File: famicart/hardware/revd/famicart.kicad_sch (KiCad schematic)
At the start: 134 parts, among them J1 Famicom 60-pin edge, J2 RUN/GND, J3 USB-C PRG/mapper (U1) (HRO TY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, J4 USB-C CHR (U2) (HRO TYPE-C-31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, J5 SWD A (SWCLK GND SWDIO), J6 SWD B (SWCLK GND SWDIO), SW1 RESET, SW2 BOOTSEL A, SW3 BOOTSEL B, U1 RP2350B, U10 74LVC541 U10, U11 74LVC541 U11, U12 74LVC245 CPU data (console<->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, U13 74LVC1G11 AND3: CPU data enab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, U14 74LVC1G32 OR: CPU 245 /OE, U15 74LVC1G04 INV: R/W, U16 74LVC1G00 NAND: WRAM /WE, U17 74LVC541 U17, U18 74LVC541 U18, U19 74LVC245 PPU data (console<->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, U2 RP2350B, U20 74LVC00 PPU access / CIRAM gl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, U21 74LVC1G32 OR: PPU 245 /OE, U22 74LVC139 CHR ROM/RAM select, U24 74LVC245 CPU->PPU data bridge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, U26 74LVC1G07 OD: /IRQ A, U27 74LVC1G07 OD: /IRQ B, U28 AMS1117-3.3, U3 W25Q16JVSSIQ, U4 W25Q16JVSSIQ, U5 S29GL01GS 1Gbit NOR (x8 use), U6 S29GL01GS 1Gbit NOR (x8 use), U7 IS62WV5128 512Kx8 SRAM, U8 IS62WV5128 512Kx8 SRAM, U9 74LVC541 U9, Y1 12MHz ABM8-272-T3, Y2 12MHz ABM8-272-T3

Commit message: famicart rev D: boot-bank pull-ups, F-RAM save RAM, U1 GPIO remap for PIO-driven nDRIVE
Target is a cartridge that works in a real Famicom: PRG bank lines are pulled up so the
console boots from a fixed top bank (boot stub) before the MCUs are up; WRAM becomes a
128 KB FM28V100 F-RAM (non-volatile saves without a battery); nDRIVE moves into PIO0's
GPIO window so the data-drive path can assert it by side-set.

Co-Authored-By: Claude Fable 5.1 <noreply@anthropic.com>
Claude-Session: https://claude.ai/code/session_01RfF2rUHDV6Gz9CaznXPSPp
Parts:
- removed U7: IS62WV5128 512Kx8 SRAM, Package_SO:TSOP-I-32_11.8x8mm_P0.5mm, symbol famicart:IS62WV5128_sTSOP32
- added R26: 1k, Resistor_SMD:R_0603_1608Metric, symbol Device:R
- added RN7, RN8, RN9: 10k x4, Resistor_SMD:R_Array_Convex_4x0603, symbol Device:R_Pack04
- added U7: FM28V100 128Kx8 F-RAM (WRAM/save), Package_SO:TSOP-I-32_11.8x8mm_P0.5mm, symbol famicart:FM28V100_TSOP32
- R25: value 1k -> 10k
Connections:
- net +3V3: now also R25.2, RN7.5 (R4.2), RN7.6 (R3.2), RN7.7 (R2.2), RN7.8 (R1.2), RN8.5 (R4.2), RN8.6 (R3.2), RN8.7 (R2.2), RN8.8 (R1.2), RN9.5 (R4.2), RN9.6 (R3.2), RN9.7 (R2.2), RN9.8 (R1.2), U7.6 (CE2), U7.8 (VDD)
- net CA0: now also U7.20 (A0)
- net CA1: now also U7.19 (A1)
- net CA10: now also U7.31 (A10)
- net CA11: now also U7.1 (A11)
- net CA12: now also U7.12 (A12)
- net CA2: now also U7.18 (A2)
- net CA3: now also U7.17 (A3)
- net CA4: now also U7.16 (A4)
- net CA5: now also U7.15 (A5)
- net CA6: now also U7.14 (A6)
- net CA7: now also U7.13 (A7)
- net CA8: now also U7.3 (A8)
- net CA9: now also U7.2 (A9)
- net CD0: now also U7.21 (DQ0)
- net CD1: now also U7.22 (DQ1)
- net CD2: now also U7.23 (DQ2)
- net CD3: now also U7.25 (DQ3)
- net CD4: now also U7.26 (DQ4)
- net CD5: now also U7.27 (DQ5)
- net CD6: now also U7.28 (DQ6)
- net CD7: now also U7.29 (DQ7)
- net CRWn: now also U7.32 (OE#)
- net GND: now also U7.24 (VSS)
- net LED: now also R26.1; no longer R25.1
- net LED_A: now also R26.2; no longer R25.2
- net PRG_A13: now also U1.28 (GPIO27), RN7.1 (R1.1), U7.4 (A13); no longer U1.27 (GPIO26)
- net PRG_A14: now also U1.36 (GPIO28), RN7.2 (R2.1), U7.11 (A14); no longer U1.28 (GPIO27)
- net PRG_A15: now also U1.37 (GPIO29), RN7.3 (R3.1), U7.7 (A15); no longer U1.36 (GPIO28)
- net PRG_A16: now also U1.38 (GPIO30), RN7.4 (R4.1), U7.10 (A16); no longer U1.37 (GPIO29)
- net PRG_A17: now also U1.39 (GPIO31), RN8.1 (R1.1); no longer U1.38 (GPIO30)
- net PRG_A18: now also U1.40 (GPIO32), RN8.2 (R2.1); no longer U1.39 (GPIO31)
- net PRG_A19: now also U1.42 (GPIO33), RN8.3 (R3.1); no longer U1.40 (GPIO32)
- net PRG_A20: now also U1.43 (GPIO34), RN8.4 (R4.1); no longer U1.42 (GPIO33)
- net PRG_A21: now also U1.44 (GPIO35), RN9.1 (R1.1); no longer U1.43 (GPIO34)
- net PRG_A22: now also U1.45 (GPIO36), RN9.2 (R2.1); no longer U1.44 (GPIO35)
- net PRG_A23: now also U1.46 (GPIO37), RN9.3 (R3.1); no longer U1.45 (GPIO36)
- net PRG_A24: now also U1.47 (GPIO38), RN9.4 (R4.1); no longer U1.46 (GPIO37)
- net PRG_A25: now also R25.1, U1.48 (GPIO39); no longer U1.47 (GPIO38)
- net WRAM_nCE: now also U1.49 (GPIO40_ADC0), U7.30 (CE1#); no longer U1.48 (GPIO39)
- net WRAM_nWE: now also U7.5 (WE#)
- net nDRIVE: now also U1.27 (GPIO26); no longer U1.49 (GPIO40_ADC0)
- no-connect marks 51 -> 52

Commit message: famicart/hardware rev D: schematic with F-RAM, bridge direction, RY/BY# (board routing in progress)
Co-Authored-By: Claude Fable 5.1 <noreply@anthropic.com>
Claude-Session: https://claude.ai/code/session_01RfF2rUHDV6Gz9CaznXPSPp
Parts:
- added R27: 10k, Resistor_SMD:R_0603_1608Metric, symbol Device:R
- added R28: 1k, Resistor_SMD:R_0603_1608Metric, symbol Device:R
- R26: value 1k -> 10k
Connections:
- net +3V3: now also R26.2, R27.2; no longer U24.1 (A->B)
- net LED: now also R28.1; no longer R26.1
- net LED_A: now also R28.2; no longer R26.2
- net BRIDGE_DIR: now reaches U2.53 (GPIO42_ADC2)
- net BRIDGE_DIR: now also R26.1, U24.1 (A->B)
- net CHR_RYBY: now reaches U2.54 (GPIO43_ADC3)
- net CHR_RYBY: now also U6.17 (RY/BY#), R27.1
- no-connect marks 52 -> 49

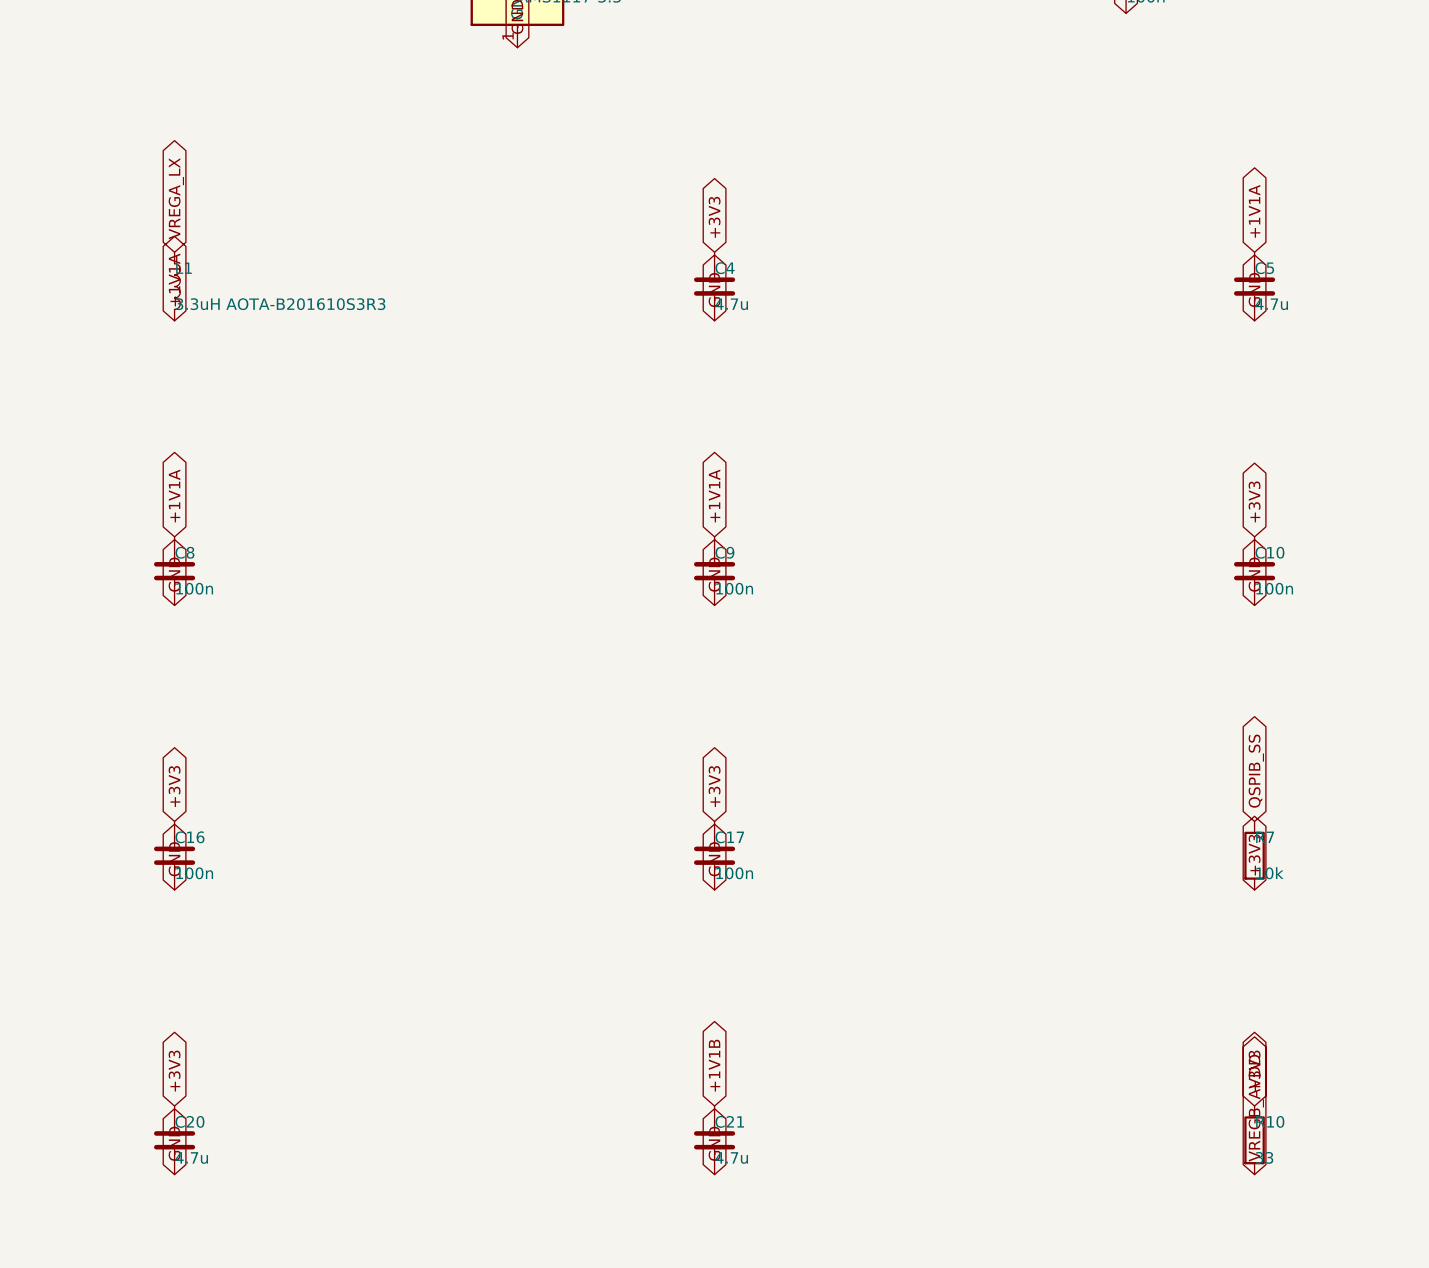
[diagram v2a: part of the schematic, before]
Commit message: famicart rev D: routed 6-layer board (0 unconnected, 0 DRC errors), gerbers, BOM, JLCPCB package
- Freerouting 1.9 (6 layers, ~30 min) -> 6 open connections, finished by finish_route.py
  (negotiated rip-up, plane vias) in 3 rounds; connectivity-safe cleanup of dangling stubs
  and duplicate vias. 6185 tracks, 609 vias; VREG_LX 1.9 mm, QSPI SCLK ~6 mm.
- hardware/revd: schematic, board, project with the board's design rules, 6-layer gerbers +
  drill, front/back/In2/In3 renders, bom.csv, jlcpcb/ (BOM with LCSC parts incl. S29GL01GS,
  FM28V100, IS62WV5128, USB-C; CPL; gerbers.zip; ordering notes for the 6-layer stack).
- gen_sch keeps a pcbnew-written project file and writes the FC_* rules; gen_jlc part keys fixed.
- docs: rev D routing result and the MCU placement rules.

Co-Authored-By: Claude Opus 5.5 <noreply@anthropic.com>
Claude-Session: https://claude.ai/code/session_01RfF2rUHDV6Gz9CaznXPSPp
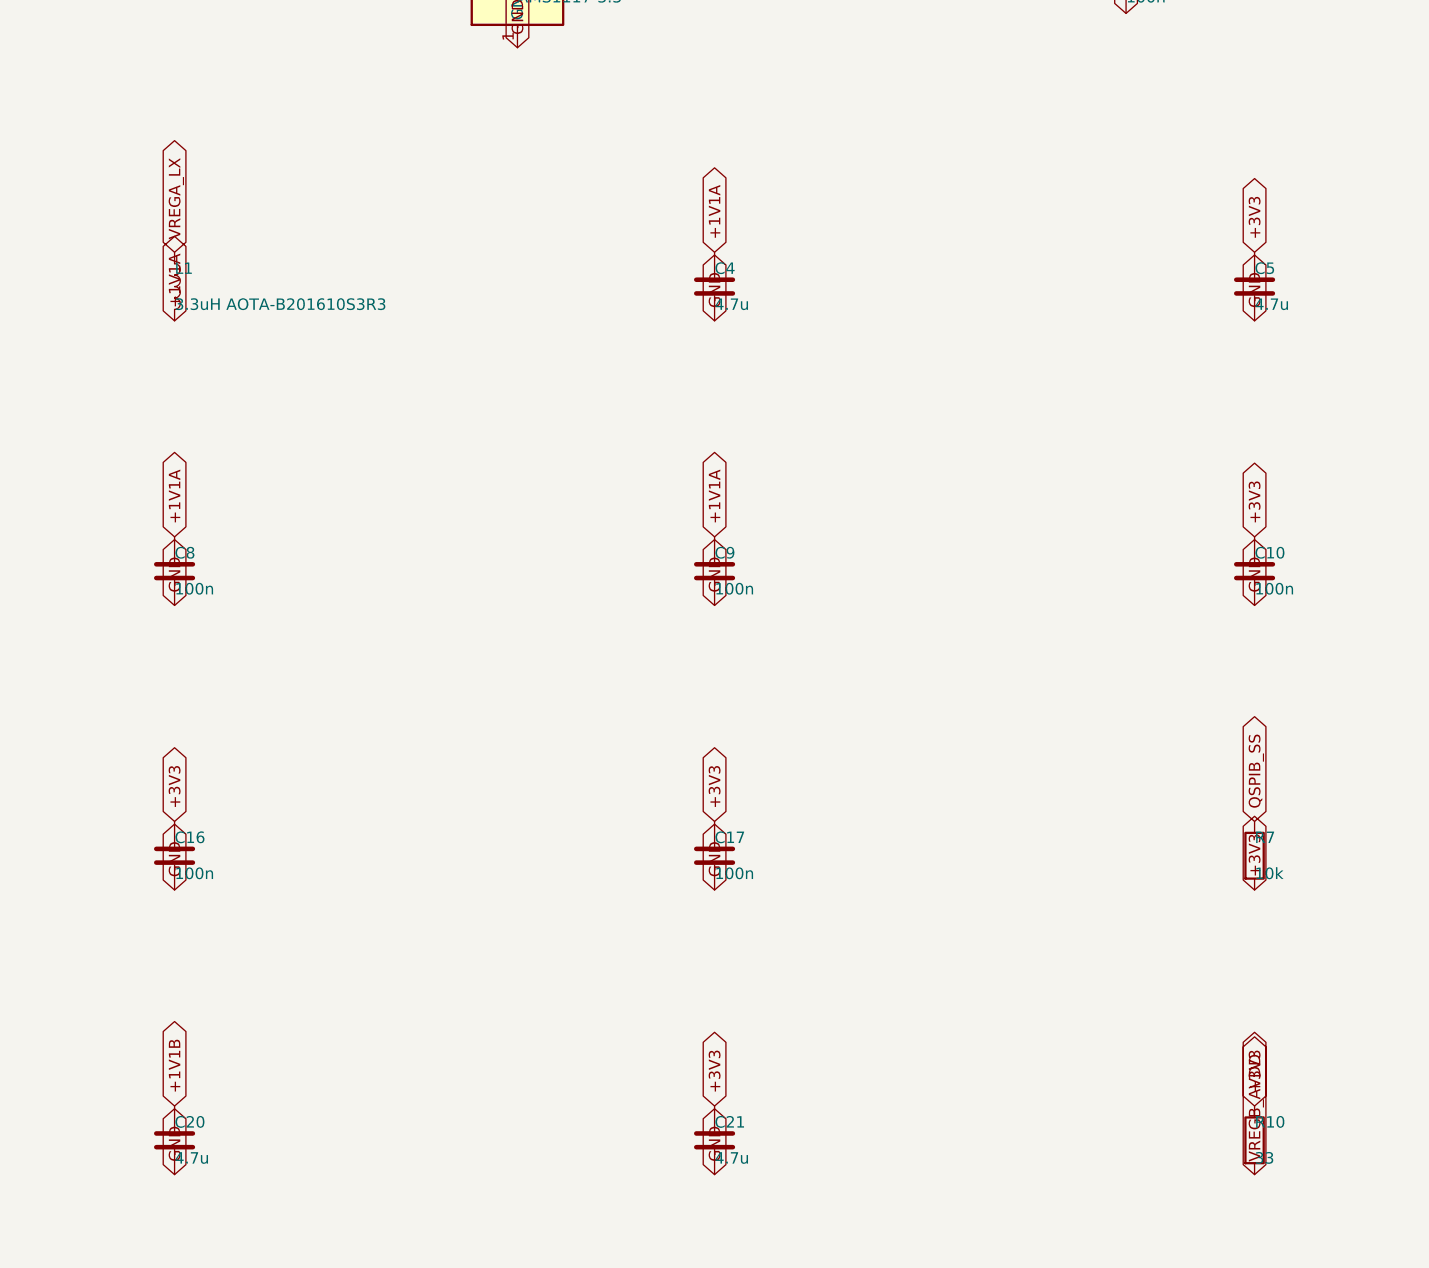
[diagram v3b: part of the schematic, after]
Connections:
- net +1V1A: now also C4.1; no longer C5.1
- net +1V1B: now also C20.1; no longer C21.1
- net +3V3: now also C21.1, C5.1; no longer C20.1, C4.1
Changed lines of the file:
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@@
     )
   )
-  (global_label "+3V3"
+  (global_label "+1V1A"
     (shape bidirectional)
     (at 370 553.64 90)
@@
     )
   )
-  (global_label "+1V1A"
+  (global_label "+3V3"
     (shape bidirectional)
     (at 430 553.64 90)
@@
     )
   )
-  (global_label "+3V3"
+  (global_label "+1V1B"
     (shape bidirectional)
     (at 310 648.5 90)
@@
     )
   )
-  (global_label "+1V1B"
+  (global_label "+3V3"
     (shape bidirectional)
     (at 370 648.5 90)
